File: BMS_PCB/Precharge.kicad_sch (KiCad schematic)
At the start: 6 parts, among them K1 Relay_SPST-NO, Q1 2N7002KT7G

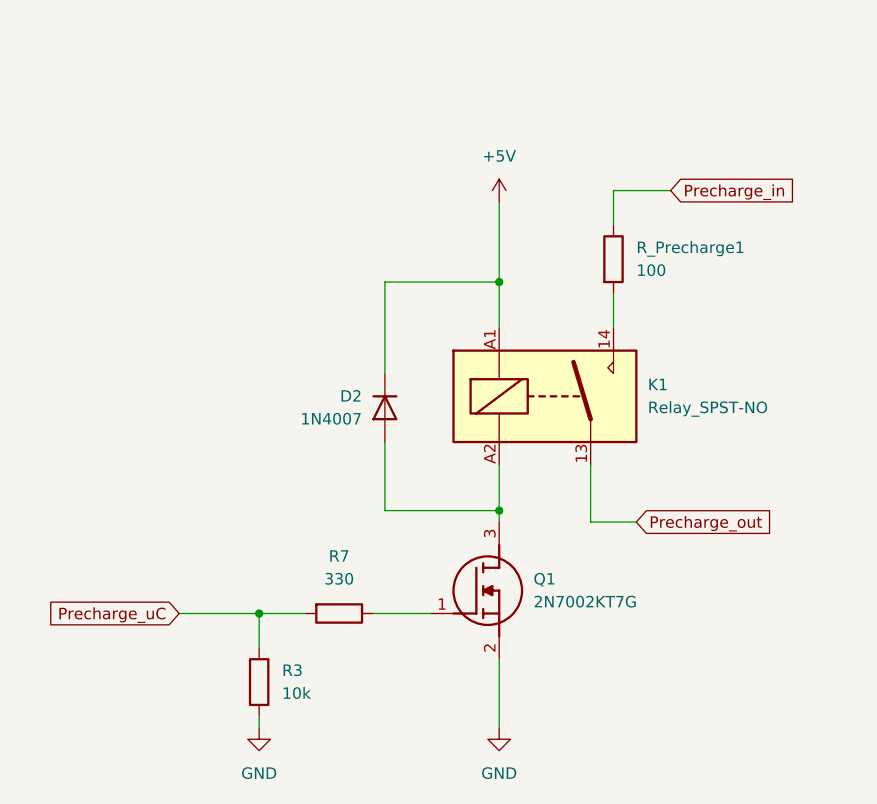
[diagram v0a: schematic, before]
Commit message: Changes Schematic
- Symbol Relais
- add DUMMY
- changed Fuses 100mA
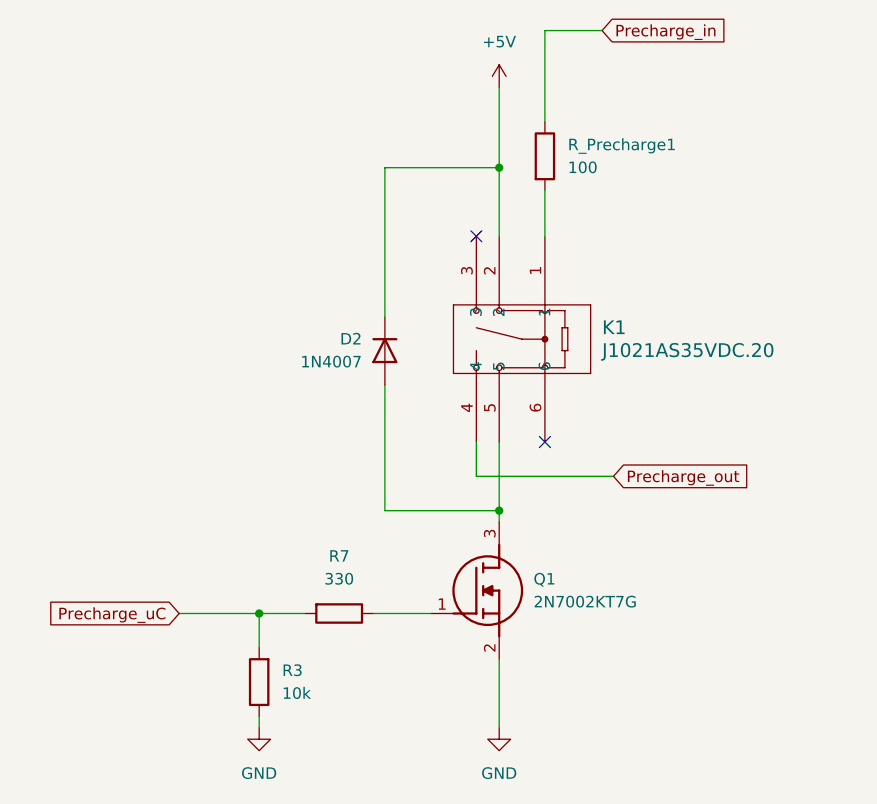
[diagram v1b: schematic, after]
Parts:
- removed K1: Relay_SPST-NO, J1021AS35VDC.20:J1021AS_CRS, symbol Relay:Relay_SPST-NO
- added K1: J1021AS35VDC.20, J1021AS35VDC.20:J1021AS_CRS, symbol J1021AS35VDC.20:J1021AS35VDC.20
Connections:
- net +5V: now also K1.2
- net Precharge_out: now also K1.4
- net at R_Precharge1.2: now also K1.1
- net at D2.2 (A), Q1.3 (D): now also K1.5
- no-connect marks 0 -> 2
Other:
- moved on the sheet: D2, R_Precharge1

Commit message: Bugfixes
noch ein paar Fehler ausgemerzt
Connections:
- net at R_Precharge1.2: now also K1.6; no longer K1.1
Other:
- moved on the sheet: R_Precharge1
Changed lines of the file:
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@@
 	)
 	(no_connect
-		(at 134.62 76.2)
+		(at 134.62 53.34)
 	)
 	(no_connect
@@
 	(wire
 		(pts
-			(xy 134.62 48.26) (xy 134.62 53.34)
+			(xy 134.62 76.2) (xy 143.51 76.2)
 		)
 		(stroke
@@
 	(wire
 		(pts
-			(xy 134.62 30.48) (xy 134.62 40.64)
-		)
-		(stroke
-			(width 0)
-			(type default)
-		)
-	)
-	(wire
-		(pts
-			(xy 140.97 30.48) (xy 134.62 30.48)
+			(xy 143.51 76.2) (xy 143.51 55.88)
+		)
+		(stroke
+			(width 0)
+			(type default)
+		)
+	)
+	(wire
+		(pts
+			(xy 143.51 38.1) (xy 143.51 48.26)
+		)
+		(stroke
+			(width 0)
+			(type default)
+		)
+	)
+	(wire
+		(pts
+			(xy 149.86 38.1) (xy 143.51 38.1)
 		)
 		(stroke
@@
 	(global_label "Precharge_in"
 		(shape input)
-		(at 140.97 30.48 0)
+		(at 149.86 38.1 0)
 		(fields_autoplaced yes)
 		(effects
@@
 		)
 		(property "Intersheetrefs" "${INTERSHEET_REFS}"
-			(at 156.2318 30.48 0)
+			(at 165.1218 38.1 0)
 			(effects
 				(font
@@
 	(symbol
 		(lib_id "Device:R")
-		(at 134.62 44.45 0)
+		(at 143.51 52.07 0)
 		(unit 1)
 		(exclude_from_sim no)
@@
 		(fields_autoplaced yes)
 		(property "Reference" "R_Precharge1"
-			(at 137.16 43.1799 0)
+			(at 146.05 50.7999 0)
 			(effects
 				(font
@@
 		)
 		(property "Value" "100"
-			(at 137.16 45.7199 0)
+			(at 146.05 53.3399 0)
 			(effects
 				(font
@@
 		)
 		(property "Footprint" "Resistor_SMD:R_2816_7142Metric_Pad3.20x4.45mm_HandSolder"
-			(at 132.842 44.45 90)
+			(at 141.732 52.07 90)
 			(effects
 				(font
@@
 		)
 		(property "Datasheet" "~"
-			(at 134.62 44.45 0)
+			(at 143.51 52.07 0)
 			(effects
 				(font
@@
 		)
 		(property "Description" "Resistor"
-			(at 134.62 44.45 0)
+			(at 143.51 52.07 0)
 			(effects
 				(font
@@
 		(dnp no)
 		(property "Reference" "K1"
-			(at 140.97 63.4999 90)
+			(at 146.05 63.5 90)
 			(effects
 				(font
@@
 		)
 		(property "Value" "J1021AS35VDC.20"
-			(at 140.97 66.0399 90)
-			(effects
-				(font
+			(at 146.05 66.04 90)
+			(effects
+				(font
